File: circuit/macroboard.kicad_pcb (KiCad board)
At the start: 2 copper layers, 91 x 88 mm, 33 parts, among them SW1 CherryMX, SW10 CherryMX, SW11 CherryMX, SW12 CherryMX, SW2 CherryMX, SW3 CherryMX, SW4 CherryMX, SW5 CherryMX, SW6 CherryMX, SW7 CherryMX, SW8 CherryMX, SW9 CherryMX, U1 ATmega32U4-A

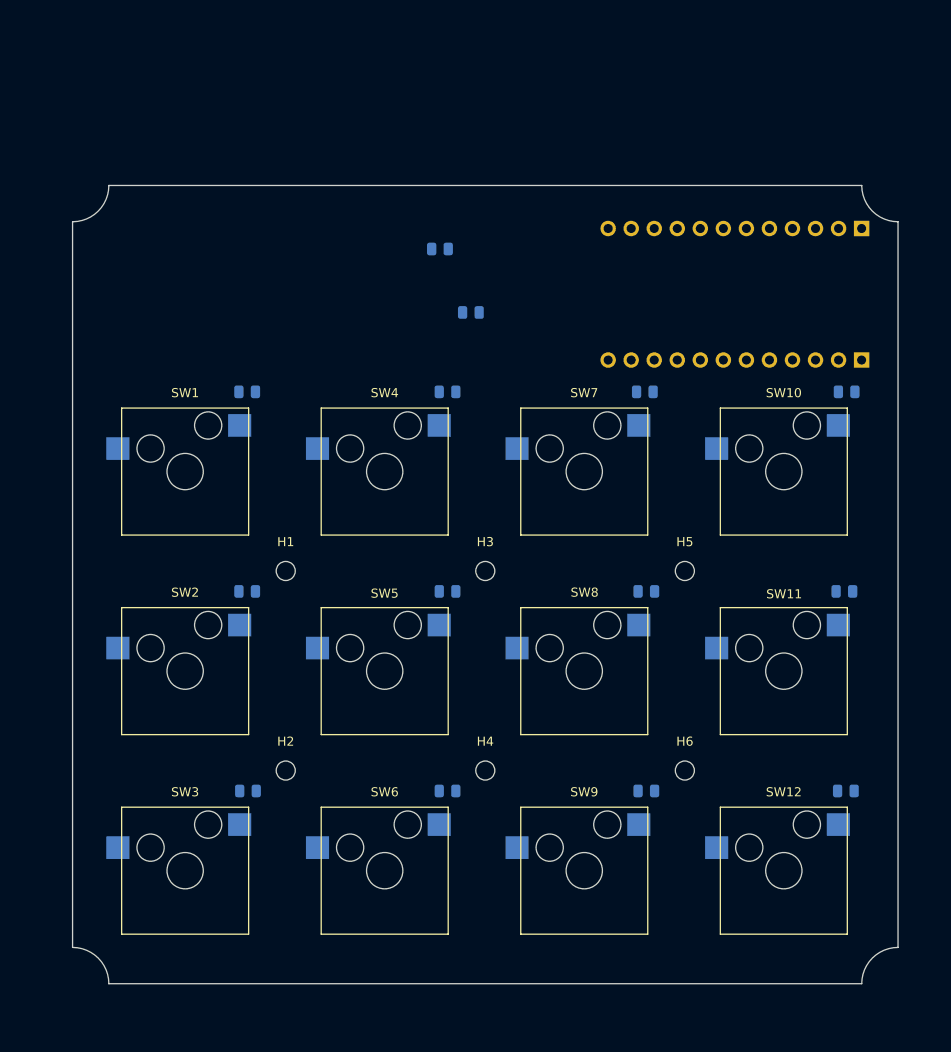
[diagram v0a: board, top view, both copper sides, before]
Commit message: add reusable debounce circuit with solder jumper
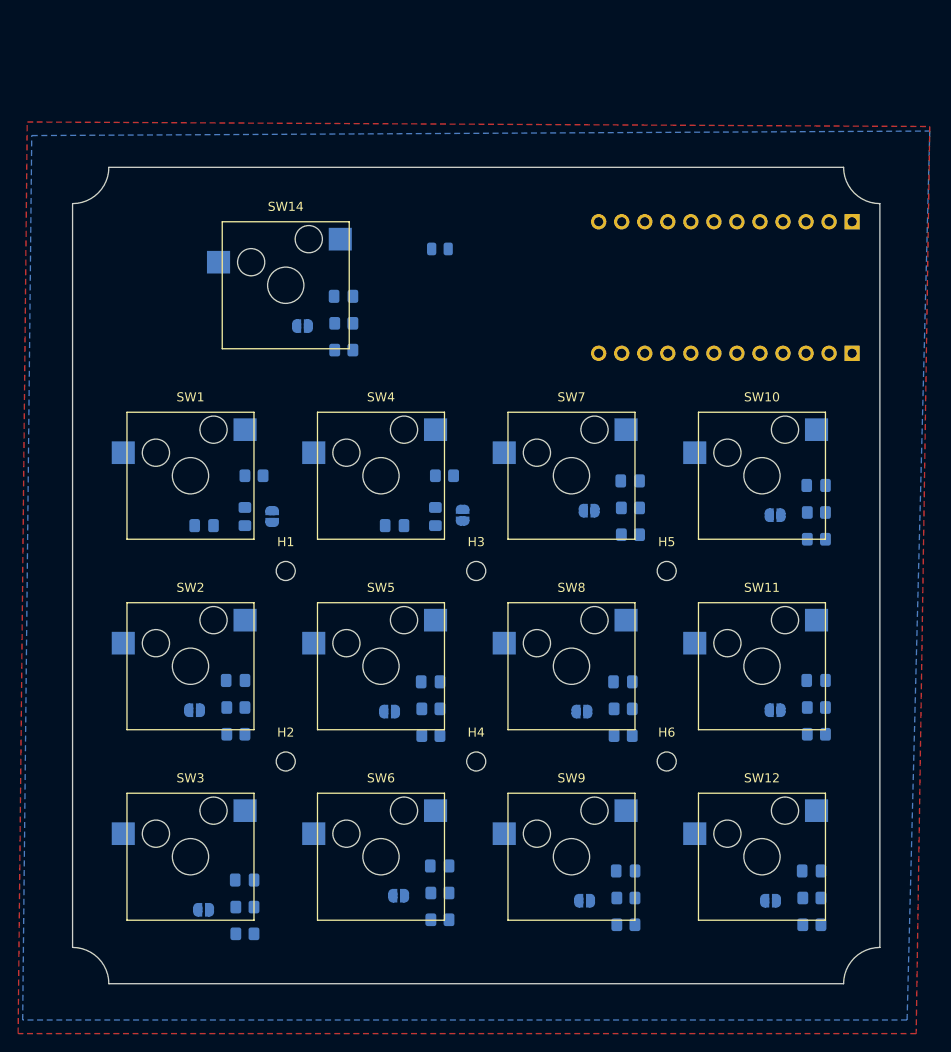
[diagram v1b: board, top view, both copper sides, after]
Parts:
- removed R10, R11, R12, R14, R2, R3, R4, R5, R6, R7, R8, R9: 10k, Resistor_SMD:R_0805_2012Metric
- added C1: 10u, Capacitor_SMD:C_0805_2012Metric_Pad1.18x1.45mm_HandSolder, B.Cu at (96.9, 60.2)
- added C10: 10u, Capacitor_SMD:C_0805_2012Metric_Pad1.18x1.45mm_HandSolder, B.Cu at (128.0, 123.6)
- added C11: 10u, Capacitor_SMD:C_0805_2012Metric_Pad1.18x1.45mm_HandSolder, B.Cu at (149.0, 81.1)
- added C12: 10u, Capacitor_SMD:C_0805_2012Metric_Pad1.18x1.45mm_HandSolder, B.Cu at (149.0, 102.6)
- added C13: 10u, Capacitor_SMD:C_0805_2012Metric_Pad1.18x1.45mm_HandSolder, B.Cu at (148.5, 123.6)
- added C2: 10u, Capacitor_SMD:C_0805_2012Metric_Pad1.18x1.45mm_HandSolder, B.Cu at (81.5, 85.5)
- added C3: 10u, Capacitor_SMD:C_0805_2012Metric_Pad1.18x1.45mm_HandSolder, B.Cu at (85.0, 102.6)
- added C4: 10u, Capacitor_SMD:C_0805_2012Metric_Pad1.18x1.45mm_HandSolder, B.Cu at (86.0, 124.6)
- added C5: 10u, Capacitor_SMD:C_0805_2012Metric_Pad1.18x1.45mm_HandSolder, B.Cu at (102.5, 85.5)
- added C6: 10u, Capacitor_SMD:C_0805_2012Metric_Pad1.18x1.45mm_HandSolder, B.Cu at (106.5, 102.7)
- added C7: 10u, Capacitor_SMD:C_0805_2012Metric_Pad1.18x1.45mm_HandSolder, B.Cu at (107.5, 123.0)
- added C8: 10u, Capacitor_SMD:C_0805_2012Metric_Pad1.18x1.45mm_HandSolder, B.Cu at (128.5, 80.6)
- added C9: 10u, Capacitor_SMD:C_0805_2012Metric_Pad1.18x1.45mm_HandSolder, B.Cu at (127.7, 102.7)
- added JP10: Jumper_2_Open, Jumper:SolderJumper-2_P1.3mm_Open_RoundedPad1.0x1.5mm, B.Cu at (123.5, 126.8)
- added JP11: Jumper_2_Open, Jumper:SolderJumper-2_P1.3mm_Open_RoundedPad1.0x1.5mm, B.Cu at (144.4, 84.3)
- added JP12: Jumper_2_Open, Jumper:SolderJumper-2_P1.3mm_Open_RoundedPad1.0x1.5mm, B.Cu at (144.4, 105.8)
- added JP13: Jumper_2_Open, Jumper:SolderJumper-2_P1.3mm_Open_RoundedPad1.0x1.5mm, B.Cu at (143.9, 126.8)
- added JP14: Jumper_2_Open, Jumper:SolderJumper-2_P1.3mm_Open_RoundedPad1.0x1.5mm, B.Cu at (92.3, 63.5)
- added JP2: Jumper_2_Open, Jumper:SolderJumper-2_P1.3mm_Open_RoundedPad1.0x1.5mm, B.Cu at (89.0, 84.5)
- added JP3: Jumper_2_Open, Jumper:SolderJumper-2_P1.3mm_Open_RoundedPad1.0x1.5mm, B.Cu at (80.5, 105.8)
- added JP4: Jumper_2_Open, Jumper:SolderJumper-2_P1.3mm_Open_RoundedPad1.0x1.5mm, B.Cu at (81.5, 127.8)
- added JP5: Jumper_2_Open, Jumper:SolderJumper-2_P1.3mm_Open_RoundedPad1.0x1.5mm, B.Cu at (110.0, 84.3)
- added JP6: Jumper_2_Open, Jumper:SolderJumper-2_P1.3mm_Open_RoundedPad1.0x1.5mm, B.Cu at (102.0, 106.0)
- added JP7: Jumper_2_Open, Jumper:SolderJumper-2_P1.3mm_Open_RoundedPad1.0x1.5mm, B.Cu at (103.0, 126.3)
- added JP8: Jumper_2_Open, Jumper:SolderJumper-2_P1.3mm_Open_RoundedPad1.0x1.5mm, B.Cu at (124.0, 83.8)
- added JP9: Jumper_2_Open, Jumper:SolderJumper-2_P1.3mm_Open_RoundedPad1.0x1.5mm, B.Cu at (123.2, 106.0)
- added R16: 1k, Resistor_SMD:R_0805_2012Metric_Pad1.20x1.40mm_HandSolder, B.Cu at (86.0, 84.5)
- added R17: 10k, Resistor_SMD:R_0805_2012Metric_Pad1.20x1.40mm_HandSolder, B.Cu at (87.0, 80.0)
- added R18: 10k, Resistor_SMD:R_0805_2012Metric_Pad1.20x1.40mm_HandSolder, B.Cu at (85.0, 105.5)
- added R19: 1k, Resistor_SMD:R_0805_2012Metric_Pad1.20x1.40mm_HandSolder, B.Cu at (85.0, 108.5)
- added R20: 10k, Resistor_SMD:R_0805_2012Metric_Pad1.20x1.40mm_HandSolder, B.Cu at (86.0, 127.5)
- added R21: 1k, Resistor_SMD:R_0805_2012Metric_Pad1.20x1.40mm_HandSolder, B.Cu at (86.0, 130.5)
- added R22: 10k, Resistor_SMD:R_0805_2012Metric_Pad1.20x1.40mm_HandSolder, B.Cu at (108.0, 80.0)
- added R23: 1k, Resistor_SMD:R_0805_2012Metric_Pad1.20x1.40mm_HandSolder, B.Cu at (107.0, 84.5)
- added R24: 10k, Resistor_SMD:R_0805_2012Metric_Pad1.20x1.40mm_HandSolder, B.Cu at (106.5, 105.7)
- added R25: 1k, Resistor_SMD:R_0805_2012Metric_Pad1.20x1.40mm_HandSolder, B.Cu at (106.5, 108.7)
- added R26: 10k, Resistor_SMD:R_0805_2012Metric_Pad1.20x1.40mm_HandSolder, B.Cu at (107.5, 126.0)
- added R27: 1k, Resistor_SMD:R_0805_2012Metric_Pad1.20x1.40mm_HandSolder, B.Cu at (107.5, 128.9)
- added R28: 10k, Resistor_SMD:R_0805_2012Metric_Pad1.20x1.40mm_HandSolder, B.Cu at (128.5, 83.5)
- added R29: 1k, Resistor_SMD:R_0805_2012Metric_Pad1.20x1.40mm_HandSolder, B.Cu at (128.5, 86.5)
- added R30: 10k, Resistor_SMD:R_0805_2012Metric_Pad1.20x1.40mm_HandSolder, B.Cu at (127.7, 105.7)
- added R31: 1k, Resistor_SMD:R_0805_2012Metric_Pad1.20x1.40mm_HandSolder, B.Cu at (127.7, 108.7)
- added R32: 10k, Resistor_SMD:R_0805_2012Metric_Pad1.20x1.40mm_HandSolder, B.Cu at (128.0, 126.5)
- added R33: 1k, Resistor_SMD:R_0805_2012Metric_Pad1.20x1.40mm_HandSolder, B.Cu at (128.0, 129.5)
- added R34: 10k, Resistor_SMD:R_0805_2012Metric_Pad1.20x1.40mm_HandSolder, B.Cu at (149.0, 84.0)
- added R35: 1k, Resistor_SMD:R_0805_2012Metric_Pad1.20x1.40mm_HandSolder, B.Cu at (149.0, 87.0)
- added R36: 10k, Resistor_SMD:R_0805_2012Metric_Pad1.20x1.40mm_HandSolder, B.Cu at (149.0, 105.5)
- added R37: 1k, Resistor_SMD:R_0805_2012Metric_Pad1.20x1.40mm_HandSolder, B.Cu at (149.0, 108.5)
- added R38: 10k, Resistor_SMD:R_0805_2012Metric_Pad1.20x1.40mm_HandSolder, B.Cu at (148.5, 126.5)
- added R39: 1k, Resistor_SMD:R_0805_2012Metric_Pad1.20x1.40mm_HandSolder, B.Cu at (148.5, 129.5)
- added RC1: 1k, Resistor_SMD:R_0805_2012Metric_Pad1.20x1.40mm_HandSolder, B.Cu at (96.9, 66.2)
- added SW14: CherryMX, CherryMX_KailhSocket:CherryMX_1.00u_KailhSocket, F.Cu at (90.5, 59.0)
- R1: footprint Resistor_SMD:R_0805_2012Metric -> Resistor_SMD:R_0805_2012Metric_Pad1.20x1.40mm_HandSolder
- moved R1 13.1 mm to (96.9, 63.2)
- moved SW12 2.86 mm to (143.0, 122.0)
- moved SW11 2.47 mm to (143.0, 101.0)
- moved SW10 2.45 mm to (143.0, 80.0)
- moved H6 2.24 mm to (132.5, 111.5)
- moved SW9 2.09 mm to (122.0, 122.0)
- moved H5 2.00 mm to (132.5, 90.5)
- moved SW3 1.65 mm to (80.0, 122.0)
- moved SW6 1.59 mm to (101.0, 122.0)
- moved SW8 1.51 mm to (122.0, 101.0)
- moved SW7 1.48 mm to (122.0, 80.0)
- moved H4 1.41 mm to (111.5, 111.5)
- moved U1 1.28 mm to (153.0, 66.5)
- moved H2 1.00 mm to (90.5, 111.5)
- moved H3 1.00 mm to (111.5, 90.5)
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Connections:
- R1 pad 2: /KEY1 -> /Switch13/Debounce1/IN
- SW1 pad 2: /KEY1 -> /Switch1/Debounce1/IN
- SW10 pad 2: /KEY10 -> /Switch10/Debounce1/IN
- SW11 pad 2: /KEY11 -> /Switch11/Debounce1/IN
- SW12 pad 2: /KEY12 -> /Switch12/Debounce1/IN
- SW2 pad 2: /KEY2 -> /Switch2/Debounce1/IN
- SW3 pad 2: /KEY3 -> /Switch3/Debounce1/IN
- SW4 pad 2: /KEY4 -> /Switch4/Debounce1/IN
- SW5 pad 2: /KEY5 -> /Switch5/Debounce1/IN
- SW6 pad 2: /KEY6 -> /Switch6/Debounce1/IN
- SW7 pad 2: /KEY7 -> /Switch7/Debounce1/IN
- SW8 pad 2: /KEY8 -> /Switch8/Debounce1/IN
- SW9 pad 2: /KEY9 -> /Switch9/Debounce1/IN
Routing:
- added copper zone on B.Cu, net GND
- added copper zone on F.Cu, net VCC
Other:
- board size 91 x 88 mm -> 89 x 90 mm

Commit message: add custom footprints, improve layout
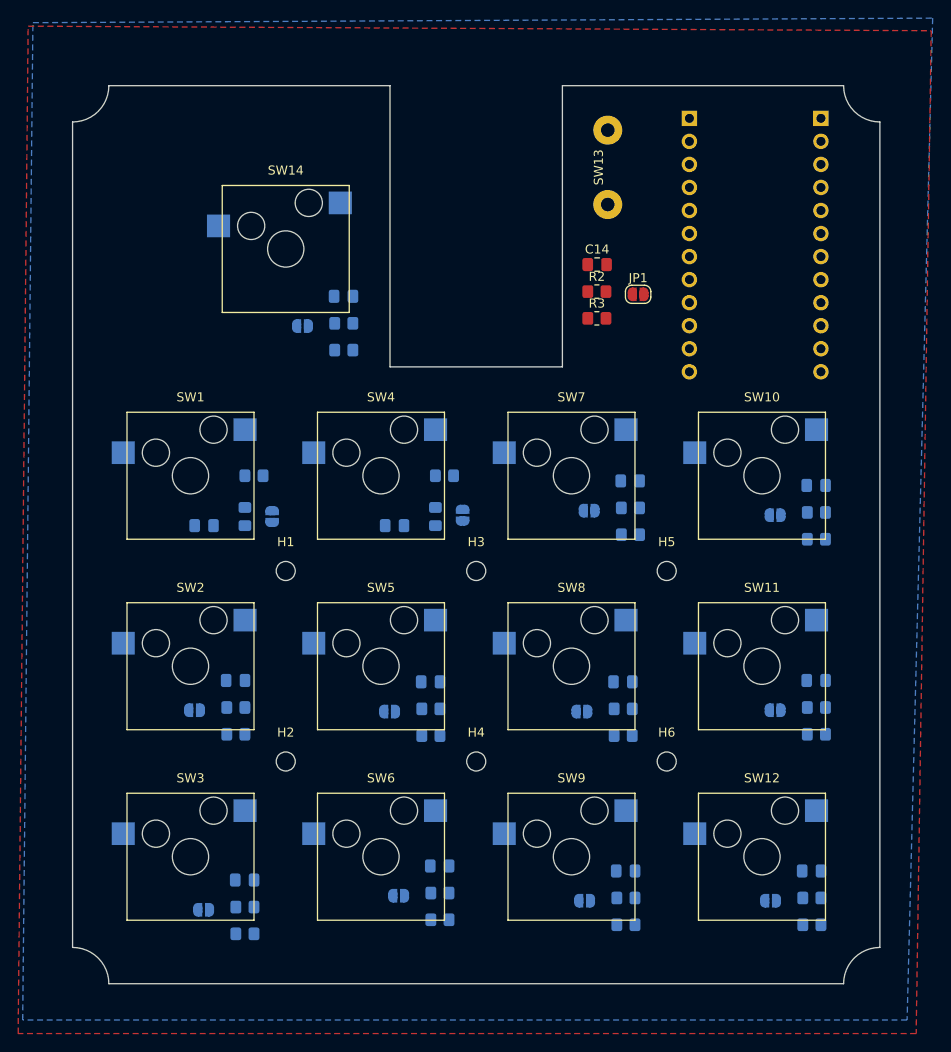
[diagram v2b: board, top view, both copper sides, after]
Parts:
- removed R13: 10k, Resistor_SMD:R_0805_2012Metric
- added C14: 10u, Capacitor_SMD:C_0805_2012Metric_Pad1.18x1.45mm_HandSolder, F.Cu at (124.8, 56.7)
- added JP1: Jumper_2_Open, Jumper:SolderJumper-2_P1.3mm_Open_RoundedPad1.0x1.5mm, F.Cu at (129.3, 60.0)
- added R2: 10k, Resistor_SMD:R_0805_2012Metric_Pad1.20x1.40mm_HandSolder, F.Cu at (124.8, 59.7)
- added R3: 1k, Resistor_SMD:R_0805_2012Metric_Pad1.20x1.40mm_HandSolder, F.Cu at (124.8, 62.6)
- added SW13: SW_Push, custom:AUX Jack 6.3mm External, F.Cu at (126.0, 46.0)
- U1: footprint MCUs:Arduino Pro Micro -> custom:Arduino Pro Micro
- moved U1 26.2 mm to (149.5, 40.5), turned to 180 degrees
- moved SW14 4.00 mm to (90.5, 55.0)
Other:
- board size 89 x 90 mm -> 89 x 99 mm

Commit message: add special switches, add routing
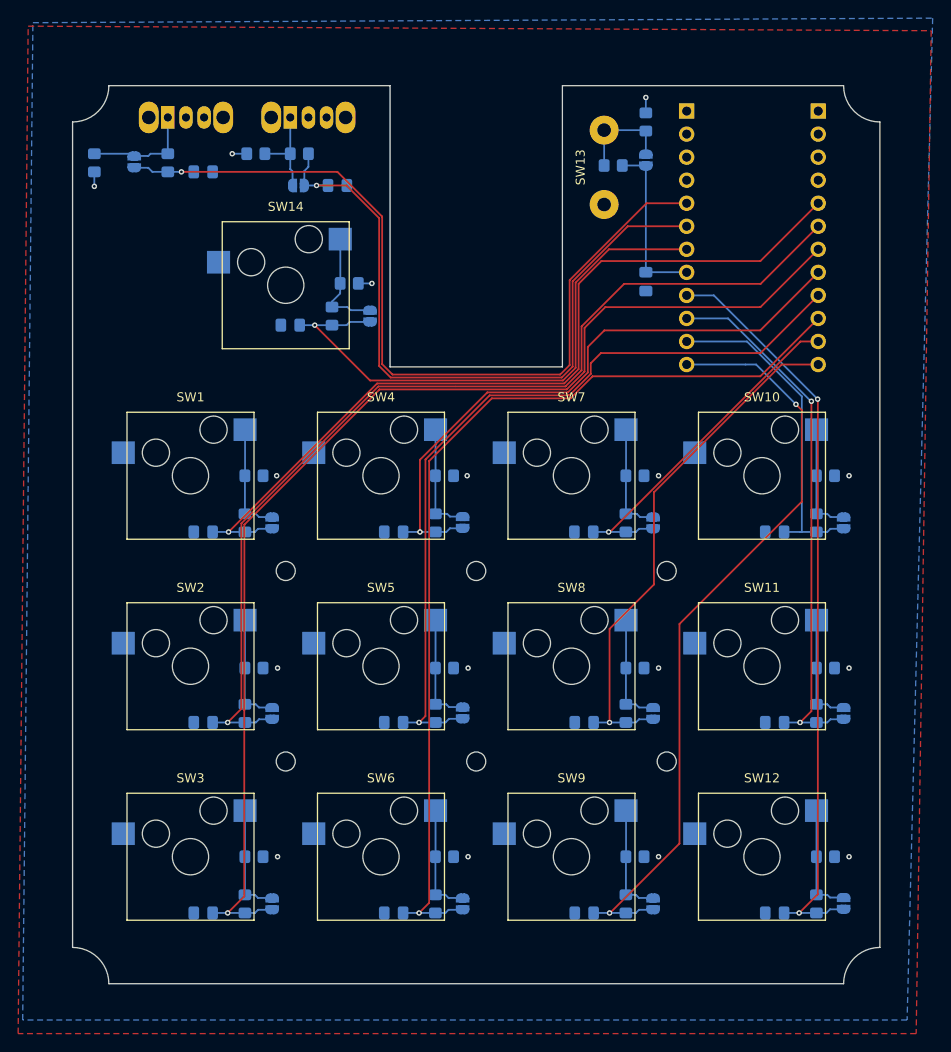
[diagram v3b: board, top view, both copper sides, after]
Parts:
- added C15: 10u, Capacitor_SMD:C_0805_2012Metric_Pad1.18x1.45mm_HandSolder, B.Cu at (96.2, 48.0)
- added C16: 10u, Capacitor_SMD:C_0805_2012Metric_Pad1.18x1.45mm_HandSolder, B.Cu at (81.4, 46.5)
- added JP15: Jumper_2_Open, Jumper:SolderJumper-2_P1.3mm_Open_RoundedPad1.0x1.5mm, B.Cu at (91.9, 48.0)
- added JP16: Jumper_2_Open, Jumper:SolderJumper-2_P1.3mm_Open_RoundedPad1.0x1.5mm, B.Cu at (73.8, 45.4)
- added R4: 10k, Resistor_SMD:R_0805_2012Metric_Pad1.20x1.40mm_HandSolder, B.Cu at (87.2, 44.5)
- added R5: 1k, Resistor_SMD:R_0805_2012Metric_Pad1.20x1.40mm_HandSolder, B.Cu at (92.0, 44.5)
- added R6: 10k, Resistor_SMD:R_0805_2012Metric_Pad1.20x1.40mm_HandSolder, B.Cu at (69.4, 45.5)
- added R7: 1k, Resistor_SMD:R_0805_2012Metric_Pad1.20x1.40mm_HandSolder, B.Cu at (77.5, 45.5)
- added SW15: SW_SPDT, Button_Switch_THT:SW_Slide_SPDT_Angled_CK_OS102011MA1Q, B.Cu at (91.0, 40.5)
- added SW16: SW_SPDT, Button_Switch_THT:SW_Slide_SPDT_Angled_CK_OS102011MA1Q, B.Cu at (77.5, 40.5)
- C14, JP1, R2, R3: moved to B.Cu
- moved R2 19.5 mm to (130.2, 41.0), turned to -90 degrees
- moved R3 16.9 mm to (126.6, 45.8)
- moved JP1 14.8 mm to (130.2, 45.2), turned to -90 degrees
- moved JP3 8.56 mm to (89.0, 106.2), turned to -90 degrees
- moved JP13 8.06 mm to (152.0, 127.2), turned to -90 degrees
- moved JP6 8.05 mm to (110.0, 106.2), turned to -90 degrees
- moved JP9 7.85 mm to (131.0, 106.2), turned to -90 degrees
- moved C8 7.60 mm to (123.4, 86.2)
- moved JP11 7.60 mm to (152.0, 85.2), turned to -90 degrees
- moved JP4 7.58 mm to (89.0, 127.2), turned to -90 degrees
- moved JP12 7.56 mm to (152.0, 106.2), turned to -90 degrees
- moved JP10 7.56 mm to (131.0, 127.2), turned to -90 degrees
- moved JP14 7.53 mm to (99.8, 62.4), turned to -90 degrees
- moved C7 7.25 mm to (102.4, 128.2)
- moved JP8 7.18 mm to (131.0, 85.2), turned to -90 degrees
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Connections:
- U1 pad 38: unconnected-(U1-PF5-Pad38) -> /SPECIAL_SWITCH_1
- U1 pad 39: unconnected-(U1-PF4-Pad39) -> /SPECIAL_SWITCH_2
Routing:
- net /KEY3: track 0.00 -> 128.9 mm, vias 0 -> 1
- net /KEY2: track 0.00 -> 109.2 mm, vias 0 -> 1
- net /KEY6: track 0.00 -> 106.4 mm, vias 0 -> 1
- net /SPECIAL_SWITCH_2: track 0.00 -> 94.8 mm, vias 0 -> 1
- net /KEY1: track 0.00 -> 92.2 mm, vias 0 -> 1
- net /KEY5: track 0.00 -> 87.5 mm, vias 0 -> 1
- net /KEY9: track 0.00 -> 85.7 mm, vias 0 -> 2
- net /KEY12: track 0.00 -> 83.4 mm, vias 0 -> 2
- net /SPECIAL_SWITCH_1: track 0.00 -> 77.6 mm, vias 0 -> 1
- net /KEY4: track 0.00 -> 68.8 mm, vias 0 -> 1
- net /MODE_SWITCH: track 0.00 -> 62.9 mm, vias 0 -> 1
- net /KEY11: track 0.00 -> 60.2 mm, vias 0 -> 2
- net /KEY8: track 0.00 -> 58.1 mm, vias 0 -> 1
- net /KEY7: track 0.00 -> 38.5 mm, vias 0 -> 1
- net /KEY10: track 0.00 -> 36.9 mm
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
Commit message: add reset switch
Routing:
- net VCC: track 6.40 -> 25.4 mm
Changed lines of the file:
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@@
 				(font
 					(size 1 1)
-					(thickness 0.1)
+					(thickness 0.15)
 				)
 			)
@@
 	)
 	(segment
+		(start 131.6 80)
+		(end 130 80)
+		(width 0.2)
+		(layer "B.Cu")
+		(net 1)
+	)
+	(segment
+		(start 131.6 101.2)
+		(end 130 101.2)
+		(width 0.2)
+		(layer "B.Cu")
+		(net 1)
+	)
+	(segment
+		(start 89.6 122)
+		(end 88 122)
+		(width 0.2)
+		(layer "B.Cu")
+		(net 1)
+	)
+	(segment
+		(start 131.6 122)
+		(end 130 122)
+		(width 0.2)
+		(layer "B.Cu")
+		(net 1)
+	)
+	(segment
 		(start 99.9 58.8)
 		(end 100 58.8)
@@
 	)
 	(segment
+		(start 89.6 101.2)
+		(end 88 101.2)
+		(width 0.2)
+		(layer "B.Cu")
+		(net 1)
+	)
+	(segment
+		(start 110.5 80)
+		(end 109 80)
+		(width 0.2)
+		(layer "B.Cu")
+		(net 1)
+	)
+	(segment
 		(start 130.2 38.3)
 		(end 130.2 40)
@@
 	)
 	(segment
+		(start 152.6 101.2)
+		(end 151 101.2)
+		(width 0.2)
+		(layer "B.Cu")
+		(net 1)
+	)
+	(segment
+		(start 152.6 80)
+		(end 151 80)
+		(width 0.2)
+		(layer "B.Cu")
+		(net 1)
+	)
+	(segment
+		(start 89.5 80)
+		(end 88 80)
+		(width 0.2)
+		(layer "B.Cu")
+		(net 1)
+	)
+	(segment
+		(start 152.6 122)
+		(end 151 122)
+		(width 0.2)
+		(layer "B.Cu")
+		(net 1)
+	)
+	(segment
+		(start 110.6 122)
+		(end 109 122)
+		(width 0.2)
+		(layer "B.Cu")
+		(net 1)
+	)
+	(segment
+		(start 110.6 101.2)
+		(end 109 101.2)
+		(width 0.2)
+		(layer "B.Cu")
+		(net 1)
+	)
+	(segment
 		(start 125.297724 56.33)
 		(end 142.83 56.33)
@@
 	)
 	(segment
-		(start 147.395 71.248862)
-		(end 147.395 86.195)
+		(start 149 86.2)
+		(end 150.2 86.2)
 		(width 0.2)
 		(layer "B.Cu")
@@
 	)
 	(segment
-		(start 134.7 65.2)
-		(end 141.346138 65.2)
+		(start 140.71 65.2)
+		(end 147.395 71.885)
 		(width 0.2)
 		(layer "B.Cu")
@@
 	)
 	(segment
-		(start 149 86.2)
-		(end 150.2 86.2)
+		(start 145.4375 86.2)
+		(end 147.2 86.2)
 		(width 0.2)
 		(layer "B.Cu")
@@
 	)
 	(segment
-		(start 145.4375 86.2)
-		(end 147.2 86.2)
+		(start 147.2 86.2)
+		(end 147.39 86.2)
 		(width 0.2)
 		(layer "B.Cu")
@@
 	)
 	(segment
-		(start 147.2 86.2)
+		(start 147.395 86.195)
 		(end 147.39 86.2)
 		(width 0.2)
@@
 	)
 	(segment
-		(start 141.346138 65.2)
-		(end 147.395 71.248862)
+		(start 147.395 71.885)
+		(end 147.395 86.195)
 		(width 0.2)
 		(layer "B.Cu")
@@
 	)
 	(segment
-		(start 147.395 86.195)
-		(end 147.39 86.2)
+		(start 134.7 65.2)
+		(end 140.71 65.2)
 		(width 0.2)
 		(layer "B.Cu")
@@
 	)
 	(segment
-		(start 147.2 107.2)
-		(end 148.45 105.95)
+		(start 148.45 105.95)
+		(end 147.2 107.2)
 		(width 0.2)
 		(layer "F.Cu")
@@
 	)
 	(segment
-		(start 148.45 105.95)
-		(end 148.45 71.79)
+		(start 148.45 72.55)
+		(end 148.45 105.95)
 		(width 0.2)
 		(layer "F.Cu")
@@
 	)
 	(via
-		(at 148.45 71.79)
+		(at 148.45 72.55)
 		(size 0.6)
 		(drill 0.3)
@@
 	)
 	(segment
-		(start 148.45 71.79)
-		(end 148.4 71.79)
+		(start 148.45 72.55)
+		(end 148.4 72.5)
 		(width 0.2)
 		(layer "B.Cu")
@@
 	)
 	(segment
+		(start 148.4 72.5)
+		(end 148.4 71.79)
+		(width 0.2)
+		(layer "B.Cu")
+		(net 12)
+	)
+	(segment
 		(start 139.27 62.66)
 		(end 134.7 62.66)
@@
 	)
 	(segment
-		(start 148.4 71.79)
-		(end 139.27 62.66)
+		(start 150.2 107.2)
+		(end 150.55 106.85)
 		(width 0.2)
 		(layer "B.Cu")
@@
 	)
 	(segment
-		(start 150.2 107.2)
-		(end 150.55 106.85)
+		(start 148.4 71.79)
+		(end 139.27 62.66)
 		(width 0.2)
 		(layer "B.Cu")

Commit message: add gerber files
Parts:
- added RESET1: SW_Push, Button_Switch_THT:SW_PUSH_6mm, B.Cu at (71.5, 55.0)
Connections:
- U1 pad 13: unconnected-(U1-~{RESET}-Pad13) -> Net-(U1-~{RESET})
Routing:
- net Net-(U1-~{RESET}): track 0.00 -> 87.1 mm, vias 0 -> 2
